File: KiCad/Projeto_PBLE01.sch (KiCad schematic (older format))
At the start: 36 parts

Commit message: correção da avaliação cruzada
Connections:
- net Vcc_5v: no longer Porta_USB1.1 (VBUS)
- no-connect marks 3 -> 4
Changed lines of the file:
@@
 Wire Wire Line
 	1200 6100 1200 5850
-Text GLabel 1800 5250 2    50   Input ~ 0
-Vcc_5v
-Wire Wire Line
-	1800 5250 1500 5250
 Wire Notes Line
 	5950 4850 5950 6500
@@
 Wire Wire Line
 	10050 5950 10300 5950
+NoConn ~ 1500 5250
 $EndSCHEMATC

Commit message: Finalização do esquemático
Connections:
- net Vbus_Externo: now reaches Porta_USB1.1 (VBUS)
- no-connect marks 4 -> 3
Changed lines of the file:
@@
 Text Label 8950 1650 2    50   ~ 0
 USB_R_Led
-$Sheet
-S 9050 850  1250 1000
-U 60BE4F2F
-F0 "Conversor_UART_USB" 50
-F1 "Conversor_UART_USB.sch" 50
-F2 "Rx" I L 9050 1050 50
-F3 "Tx" O L 9050 1150 50
-F4 "RTS" B L 9050 1250 50
-F5 "CTS" B L 9050 1350 50
-F6 "Rx_LED" B L 9050 1650 50
-F7 "Tx_LED" B L 9050 1750 50
-F8 "D-" B R 10300 1150 50
-F9 "D+" B R 10300 1000 50
-$EndSheet
 Wire Wire Line
 	8700 1350 9050 1350
@@
 Wire Wire Line
 	10050 5950 10300 5950
-NoConn ~ 1500 5250
+$Sheet
+S 9050 850  1250 1000
+U 60BE4F2F
+F0 "Conversor_UART_USB" 50
+F1 "Conversor_UART_USB.sch" 50
+F2 "Rx" I L 9050 1050 50
+F3 "Tx" O L 9050 1150 50
+F4 "RTS" B L 9050 1250 50
+F5 "CTS" B L 9050 1350 50
+F6 "Rx_LED" B L 9050 1650 50
+F7 "Tx_LED" B L 9050 1750 50
+F8 "D-" B R 10300 1150 50
+F9 "D+" B R 10300 1000 50
+F10 "Vbus" U R 10300 1650 50
+$EndSheet
+Text Label 10350 1650 0    50   ~ 0
+Vbus_Externo
+Wire Wire Line
+	10300 1650 10350 1650
+Text Label 1700 5250 0    50   ~ 0
+Vbus_Externo
+Wire Wire Line
+	1500 5250 1700 5250
 $EndSCHEMATC

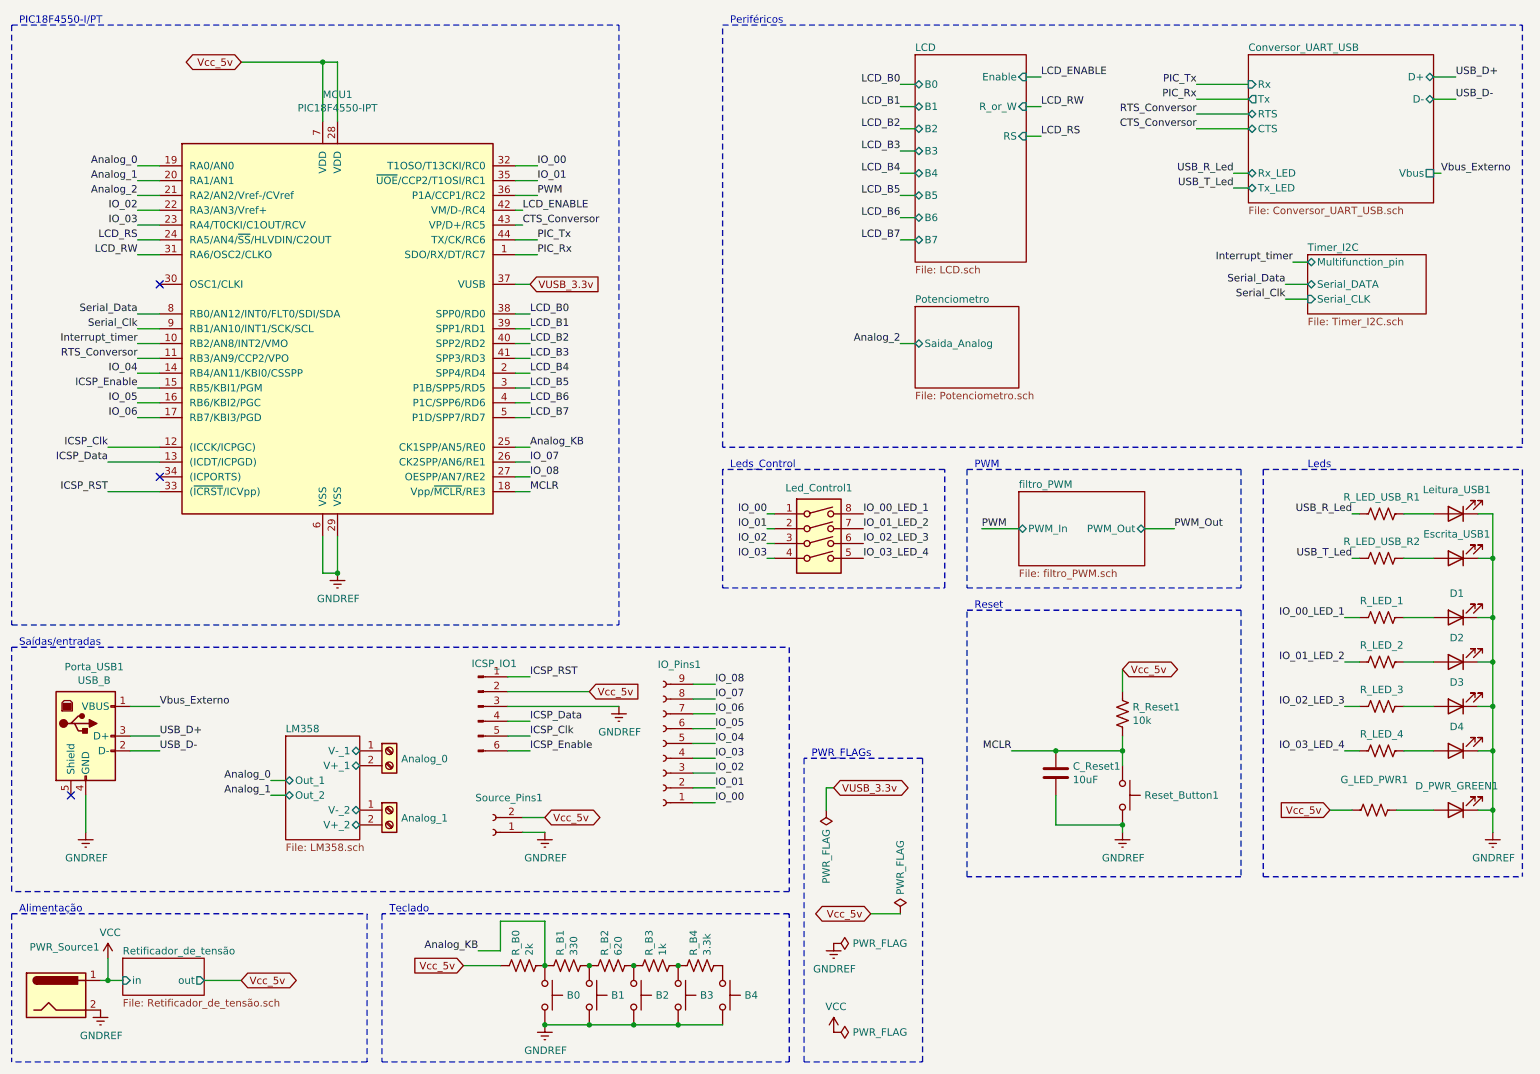
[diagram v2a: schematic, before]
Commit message: adição departe dos footprints
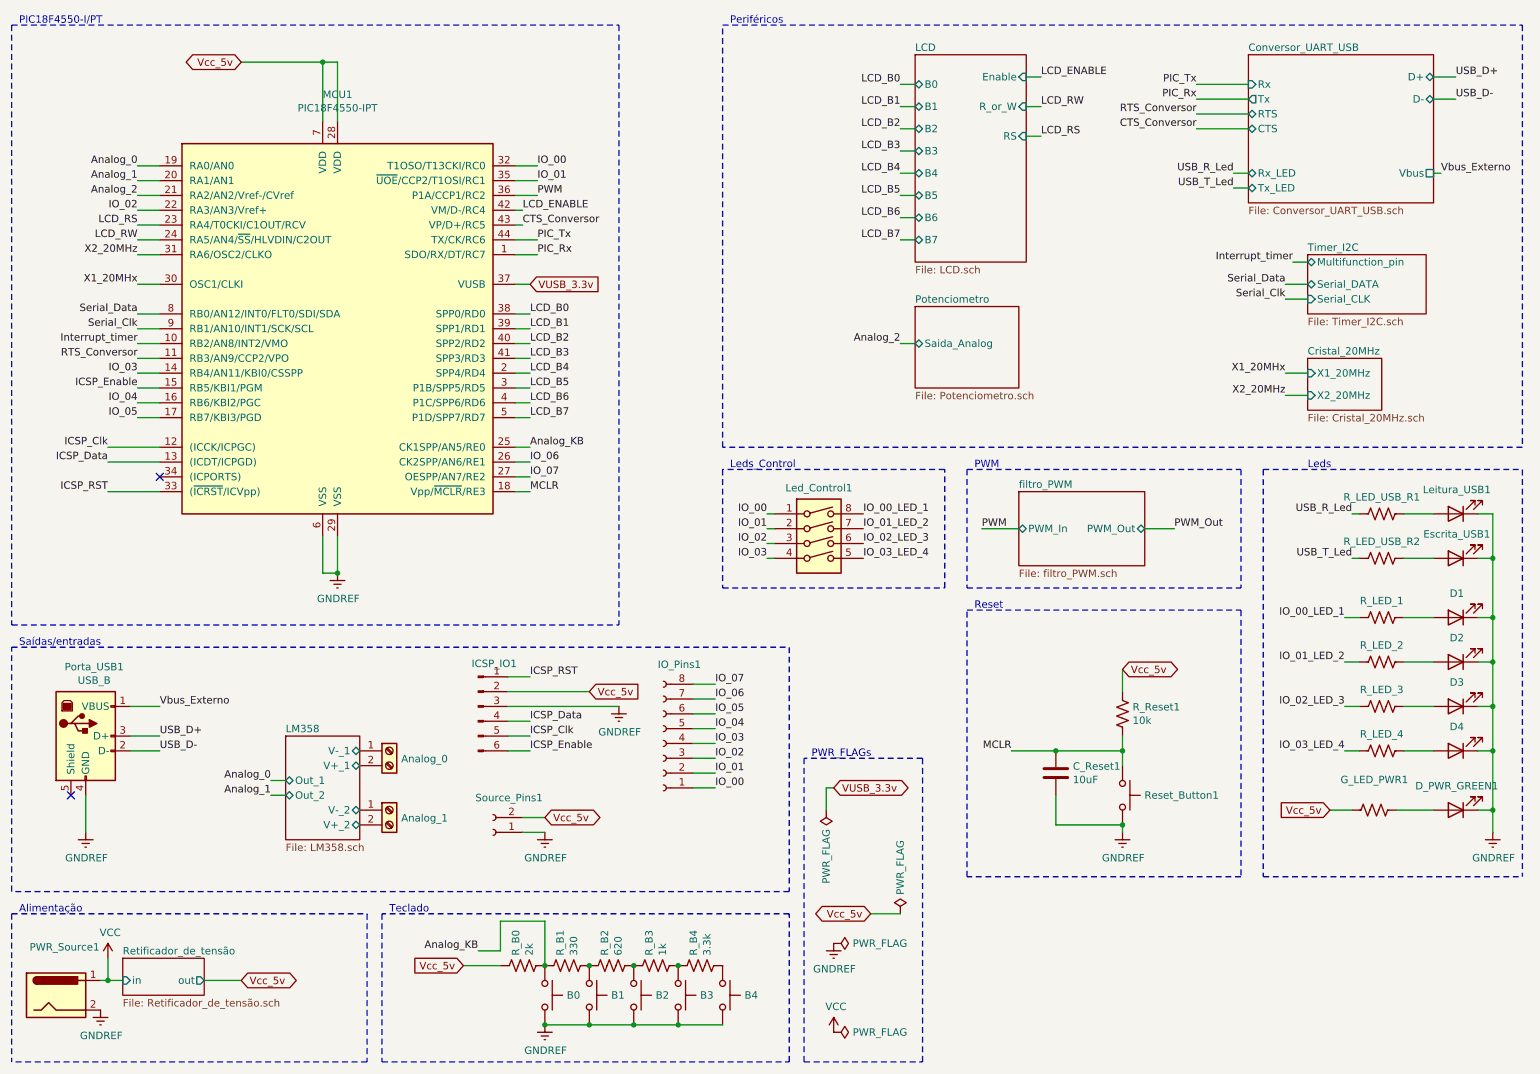
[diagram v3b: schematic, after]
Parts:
- removed IO_Pins1: Conn_01x09_Female, symbol Connector:Conn_01x09_Female
- added IO_Pins1: Conn_01x08_Female, Connector_PinHeader_1.00mm:PinHeader_1x08_P1.00mm_Vertical, symbol Connector:Conn_01x08_Female
- B0, B1, B2, B3, B4: footprint (none) -> Button_Switch_THT:SW_PUSH_6mm
- ICSP_IO1: footprint (none) -> Connector_PinHeader_1.00mm:PinHeader_1x06_P1.00mm_Vertical
- Porta_USB1: footprint (none) -> Connector_USB:USB_B_OST_USB-B1HSxx_Horizontal
- R_B0, R_B1, R_B2, R_B3, R_B4, R_LED_1, R_LED_2, R_LED_3, R_LED_4, R_LED_USB_R1, R_LED_USB_R2, R_Reset1, Reset_Button1: footprint (none) -> Resistor_SMD:R_0805_2012Metric
- Source_Pins1: footprint (none) -> Connector_PinHeader_1.00mm:PinHeader_1x02_P1.00mm_Vertical
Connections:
- net IO_08 is gone; now on net IO_07: MCU1.27 (OESPP/AN7/RE2)
- net IO_00: now also IO_Pins1.1 (Pin_1)
- net IO_01: now also IO_Pins1.2 (Pin_2)
- net IO_02: now also IO_Pins1.3 (Pin_3)
- net IO_03: now also MCU1.14 (RB4/AN11/KBI0/CSSPP), IO_Pins1.4 (Pin_4); no longer MCU1.23 (RA4/T0CKI/C1OUT/RCV)
- net IO_04: now also MCU1.16 (RB6/KBI2/PGC), IO_Pins1.5 (Pin_5); no longer MCU1.14 (RB4/AN11/KBI0/CSSPP)
- net IO_05: now also MCU1.17 (RB7/KBI3/PGD), IO_Pins1.6 (Pin_6); no longer MCU1.16 (RB6/KBI2/PGC)
- net IO_06: now also MCU1.26 (CK2SPP/AN6/RE1), IO_Pins1.7 (Pin_7); no longer MCU1.17 (RB7/KBI3/PGD)
- net IO_07: now also IO_Pins1.8 (Pin_8); no longer MCU1.26 (CK2SPP/AN6/RE1)
- net LCD_RS: now also MCU1.23 (RA4/T0CKI/C1OUT/RCV); no longer MCU1.24 (RA5/AN4/~SS~/HLVDIN/C2OUT)
- net LCD_RW: now also MCU1.24 (RA5/AN4/~SS~/HLVDIN/C2OUT); no longer MCU1.31 (RA6/OSC2/CLKO)
- net X1_20MHx: now reaches MCU1.30 (OSC1/CLKI)
- new net X2_20MHz: MCU1.31 (RA6/OSC2/CLKO)
- no-connect marks 3 -> 2
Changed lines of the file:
@@
 $Descr A4 11693 8268
 encoding utf-8
-Sheet 1 9
+Sheet 1 10
 Title ""
 Date ""
@@
 F 0 "Porta_USB1" H 1257 5917 50  0000 C CNN
 F 1 "USB_B" H 1257 5826 50  0000 C CNN
-F 2 "" H 1350 5400 50  0001 C CNN
+F 2 "Connector_USB:USB_B_OST_USB-B1HSxx_Horizontal" H 1350 5400 50  0001 C CNN
 F 3 " ~" H 1350 5400 50  0001 C CNN
 	1    1200 5450
@@
 F 0 "R_LED_USB_R1" V 9837 3950 50  0000 C CNN
 F 1 "100" V 9837 3950 50  0001 C CNN
-F 2 "" V 9990 3940 50  0001 C CNN
+F 2 "Resistor_SMD:R_0805_2012Metric" V 9990 3940 50  0001 C CNN
 F 3 "~" H 9950 3950 50  0001 C CNN
 	1    9950 3950
@@
 F 0 "R_Reset1" H 8268 5346 50  0000 L CNN
 F 1 "10k" H 8268 5255 50  0000 L CNN
-F 2 "" V 8240 5290 50  0001 C CNN
+F 2 "Resistor_SMD:R_0805_2012Metric" V 8240 5290 50  0001 C CNN
 F 3 "~" H 8200 5300 50  0001 C CNN
 	1    8200 5300
@@
 F 0 "Reset_Button1" V 8200 5998 50  0000 L CNN
 F 1 "SW_Push" V 8245 5998 50  0001 L CNN
-F 2 "" H 8200 6050 50  0001 C CNN
+F 2 "Resistor_SMD:R_0805_2012Metric" H 8200 6050 50  0001 C CNN
 F 3 "~" H 8200 6050 50  0001 C CNN
 	1    8200 5850
@@
 F 0 "R_LED_USB_R2" V 9837 4250 50  0000 C CNN
 F 1 "100" V 9837 4250 50  0001 C CNN
-F 2 "" V 9990 4240 50  0001 C CNN
+F 2 "Resistor_SMD:R_0805_2012Metric" V 9990 4240 50  0001 C CNN
 F 3 "~" H 9950 4250 50  0001 C CNN
 	1    9950 4250
@@
 F 0 "B0" V 4300 7348 50  0000 L CNN
 F 1 "SW_Push" V 4345 7348 50  0001 L CNN
-F 2 "" H 4300 7400 50  0001 C CNN
+F 2 "Button_Switch_THT:SW_PUSH_6mm" H 4300 7400 50  0001 C CNN
 F 3 "~" H 4300 7400 50  0001 C CNN
 	1    4300 7200
@@
 F 0 "B1" V 4600 7348 50  0000 L CNN
 F 1 "SW_Push" V 4645 7348 50  0001 L CNN
-F 2 "" H 4600 7400 50  0001 C CNN
+F 2 "Button_Switch_THT:SW_PUSH_6mm" H 4600 7400 50  0001 C CNN
 F 3 "~" H 4600 7400 50  0001 C CNN
 	1    4600 7200
@@
 F 0 "B2" V 4900 7348 50  0000 L CNN
 F 1 "SW_Push" V 4945 7348 50  0001 L CNN
-F 2 "" H 4900 7400 50  0001 C CNN
+F 2 "Button_Switch_THT:SW_PUSH_6mm" H 4900 7400 50  0001 C CNN
 F 3 "~" H 4900 7400 50  0001 C CNN
 	1    4900 7200
@@
 F 0 "B3" V 5200 7348 50  0000 L CNN
 F 1 "SW_Push" V 5245 7348 50  0001 L CNN
-F 2 "" H 5200 7400 50  0001 C CNN
+F 2 "Button_Switch_THT:SW_PUSH_6mm" H 5200 7400 50  0001 C CNN
 F 3 "~" H 5200 7400 50  0001 C CNN
 	1    5200 7200
@@
 F 0 "B4" V 5500 7348 50  0000 L CNN
 F 1 "SW_Push" V 5545 7348 50  0001 L CNN
-F 2 "" H 5500 7400 50  0001 C CNN
+F 2 "Button_Switch_THT:SW_PUSH_6mm" H 5500 7400 50  0001 C CNN
 F 3 "~" H 5500 7400 50  0001 C CNN
 	1    5500 7200
@@
 F 0 "R_B1" H 4518 7046 50  0000 L CNN
 F 1 "330" H 4518 6955 50  0000 L CNN
-F 2 "" V 4490 6990 50  0001 C CNN
+F 2 "Resistor_SMD:R_0805_2012Metric" V 4490 6990 50  0001 C CNN
 F 3 "~" H 4450 7000 50  0001 C CNN
 	1    4450 7000
@@
 F 0 "R_B2" H 4818 7046 50  0000 L CNN
 F 1 "620" H 4818 6955 50  0000 L CNN
-F 2 "" V 4790 6990 50  0001 C CNN
+F 2 "Resistor_SMD:R_0805_2012Metric" V 4790 6990 50  0001 C CNN
 F 3 "~" H 4750 7000 50  0001 C CNN
 	1    4750 7000
@@
 F 0 "R_B3" H 5118 7046 50  0000 L CNN
 F 1 "1k" H 5118 6955 50  0000 L CNN
-F 2 "" V 5090 6990 50  0001 C CNN
+F 2 "Resistor_SMD:R_0805_2012Metric" V 5090 6990 50  0001 C CNN
 F 3 "~" H 5050 7000 50  0001 C CNN
 	1    5050 7000
@@
 F 0 "R_B4" H 5418 7046 50  0000 L CNN
 F 1 "3.3k" H 5418 6955 50  0000 L CNN
-F 2 "" V 5390 6990 50  0001 C CNN
+F 2 "Resistor_SMD:R_0805_2012Metric" V 5390 6990 50  0001 C CNN
 F 3 "~" H 5350 7000 50  0001 C CNN
 	1    5350 7000
@@
 F 0 "R_B0" H 4218 7046 50  0000 L CNN
 F 1 "2k" H 4218 6955 50  0000 L CNN
-F 2 "" V 4190 6990 50  0001 C CNN
+F 2 "Resistor_SMD:R_0805_2012Metric" V 4190 6990 50  0001 C CNN
 F 3 "~" H 4150 7000 50  0001 C CNN
 	1    4150 7000
@@
 F 0 "R_LED_1" V 9837 4650 50  0000 C CNN
 F 1 "100" V 9837 4650 50  0001 C CNN
-F 2 "" V 9990 4640 50  0001 C CNN
+F 2 "Resistor_SMD:R_0805_2012Metric" V 9990 4640 50  0001 C CNN
 F 3 "~" H 9950 4650 50  0001 C CNN
 	1    9950 4650
@@
 F 0 "R_LED_2" V 9837 4950 50  0000 C CNN
 F 1 "100" V 9837 4950 50  0001 C CNN
-F 2 "" V 9990 4940 50  0001 C CNN
+F 2 "Resistor_SMD:R_0805_2012Metric" V 9990 4940 50  0001 C CNN
 F 3 "~" H 9950 4950 50  0001 C CNN
 	1    9950 4950
@@
 F 0 "R_LED_3" V 9837 5250 50  0000 C CNN
 F 1 "100" V 9837 5250 50  0001 C CNN
-F 2 "" V 9990 5240 50  0001 C CNN
+F 2 "Resistor_SMD:R_0805_2012Metric" V 9990 5240 50  0001 C CNN
 F 3 "~" H 9950 5250 50  0001 C CNN
 	1    9950 5250
@@
 F 0 "R_LED_4" V 9837 5550 50  0000 C CNN
 F 1 "100" V 9837 5550 50  0001 C CNN
-F 2 "" V 9990 5540 50  0001 C CNN
+F 2 "Resistor_SMD:R_0805_2012Metric" V 9990 5540 50  0001 C CNN
 F 3 "~" H 9950 5550 50  0001 C CNN
 	1    9950 5550
@@
 F 0 "Source_Pins1" H 3842 5867 50  0000 C CNN
 F 1 "Conn_01x02_Female" H 3842 5866 50  0001 C CNN
-F 2 "" H 3950 6100 50  0001 C CNN
+F 2 "Connector_PinHeader_1.00mm:PinHeader_1x02_P1.00mm_Vertical" H 3950 6100 50  0001 C CNN
 F 3 "~" H 3950 6100 50  0001 C CNN
 	1    3950 6100
@@
 Wire Wire Line
 	1550 1600 1700 1600
-Text Label 1550 3000 2    50   ~ 0
+Text Label 1550 3200 2    50   ~ 0
 IO_04
-Text Label 1550 3200 2    50   ~ 0
+Text Label 1550 3300 2    50   ~ 0
 IO_05
-Text Label 1550 3300 2    50   ~ 0
+Text Label 4200 3600 0    50   ~ 0
 IO_06
 Wire Wire Line
-	1550 3000 1700 3000
+	1550 3200 1700 3200
+Text Label 1550 2000 2    50   ~ 0
+LCD_RS
 Text Label 1550 2100 2    50   ~ 0
-LCD_RS
-Text Label 1550 2200 2    50   ~ 0
 LCD_RW
 Wire Wire Line
+	1550 2000 1700 2000
+Wire Wire Line
 	1550 2100 1700 2100
-Wire Wire Line
-	1550 2200 1700 2200
 Wire Wire Line
 	4100 1900 4150 1900
@@
 Wire Wire Line
 	1550 3100 1700 3100
-NoConn ~ 1700 2400
 Text Label 4200 3500 0    50   ~ 0
 Analog_KB
@@
 	4100 3500 4200 3500
 Wire Wire Line
-	1550 2000 1700 2000
-Wire Wire Line
-	1550 3200 1700 3200
-Text Label 4200 3600 0    50   ~ 0
-IO_07
-Wire Wire Line
-	4100 3600 4200 3600
+	1550 3000 1700 3000
 Wire Wire Line
 	1550 3300 1700 3300
 Text Label 4200 3700 0    50   ~ 0
-IO_08
+IO_07
+Wire Wire Line
+	4100 3700 4200 3700
 Text Label 4250 1800 0    50   ~ 0
 PWM
@@
 	1    0    0    -1
 $EndComp
+Text Label 5450 5700 0    50   ~ 0
+IO_01
 Text Label 5450 5800 0    50   ~ 0
-IO_01
-Text Label 5450 5900 0    50   ~ 0
 IO_00
-Text Label 5450 5700 0    50   ~ 0
+Text Label 5450 5600 0    50   ~ 0
 IO_02
 Wire Wire Line
-	5450 5900 5300 5900
-Wire Wire Line
 	5450 5800 5300 5800
 Wire Wire Line
 	5450 5700 5300 5700
-Text Label 5450 5600 0    50   ~ 0
+Wire Wire Line
+	5450 5600 5300 5600
+Text Label 5450 5500 0    50   ~ 0
 IO_03
-Text Label 5450 5500 0    50   ~ 0
+Text Label 5450 5400 0    50   ~ 0
 IO_04
-Text Label 5450 5400 0    50   ~ 0
+Text Label 5450 5300 0    50   ~ 0
 IO_05
 Wire Wire Line
-	5300 5600 5450 5600
-Wire Wire Line
 	5300 5500 5450 5500
 Wire Wire Line
 	5300 5400 5450 5400
-Text Label 5450 5300 0    50   ~ 0
-IO_06
 Wire Wire Line
 	5300 5300 5450 5300
 Text Label 5450 5200 0    50   ~ 0
+IO_06
+Wire Wire Line
+	5300 5200 5450 5200
+Text Label 5450 5100 0    50   ~ 0
 IO_07
 Wire Wire Line
-	5300 5200 5450 5200
+	5300 5100 5450 5100
 Text Label 4200 5550 0    50   ~ 0
 ICSP_Enable
@@
 F 0 "ICSP_IO1" H 3958 5539 50  0000 C CNN
 F 1 "Conn_01x06_Male" H 3958 5540 50  0001 C CNN
-F 2 "" H 3850 5250 50  0001 C CNN
+F 2 "Connector_PinHeader_1.00mm:PinHeader_1x06_P1.00mm_Vertical" H 3850 5250 50  0001 C CNN
 F 3 "~" H 3850 5250 50  0001 C CNN
 	1    3850 5250
@@
 Text Label 1550 1900 2    50   ~ 0
 IO_02
-Text Label 1550 2000 2    50   ~ 0
+Text Label 1550 3000 2    50   ~ 0
 IO_03
-$Comp
-L Connector:Conn_01x09_Female IO_Pins1
-U 1 1 610BFF1D
-P 5100 5500
-F 0 "IO_Pins1" H 4992 4967 50  0000 C CNN
-F 1 "Conn_01x09_Female" H 4992 4966 50  0001 C CNN
-F 2 "" H 5100 5500 50  0001 C CNN
-F 3 "~" H 5100 5500 50  0001 C CNN
-	1    5100 5500
-	-1   0    0    1
-$EndComp
-Text Label 5450 5100 0    50   ~ 0
-IO_08
-Wire Wire Line
-	5450 5100 5300 5100
 $Sheet
 S 2550 5450 500  700
@@
 F7 "Out_1" B L 2550 5750 50
 $EndSheet
-Wire Wire Line
-	4100 3700 4200 3700
 Wire Wire Line
 	4100 1800 4250 1800
@@
 Wire Wire Line
 	1500 5250 1700 5250
+$Comp
+L Connector:Conn_01x08_Female IO_Pins1
+U 1 1 60E4B780
+P 5100 5500
+F 0 "IO_Pins1" H 4992 4967 50  0000 C CNN
+F 1 "Conn_01x08_Female" H 4992 4966 50  0001 C CNN
+F 2 "Connector_PinHeader_1.00mm:PinHeader_1x08_P1.00mm_Vertical" H 5100 5500 50  0001 C CNN
+F 3 "~" H 5100 5500 50  0001 C CNN
+	1    5100 5500
+	-1   0    0    1
+$EndComp
+Wire Wire Line
+	4100 3600 4200 3600
+$Sheet
+S 9450 2900 500  350
+U 60ED601E
+F0 "Cristal_20MHz" 50
+F1 "Cristal_20MHz.sch" 50
+F2 "X1_20MHz" I L 9450 3000 50
+F3 "X2_20MHz" I L 9450 3150 50
+$EndSheet
+Text Label 9300 3000 2    50   ~ 0
+X1_20MHx
+Text Label 9300 3150 2    50   ~ 0
+X2_20MHz
+Wire Wire Line
+	9300 3000 9450 3000
+Wire Wire Line
+	9300 3150 9450 3150
+Text Label 1550 2400 2    50   ~ 0
+X1_20MHx
+Text Label 1550 2200 2    50   ~ 0
+X2_20MHz
+Wire Wire Line
+	1550 2400 1700 2400
+Wire Wire Line
+	1550 2200 1700 2200
 $EndSCHEMATC

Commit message: adição de mais footprints
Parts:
- Analog_0, Analog_1: footprint (none) -> TerminalBlock:TerminalBlock_Altech_AK300-2_P5.00mm
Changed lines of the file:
@@
 F 0 "Analog_1" H 3330 5896 50  0000 L CNN
 F 1 "Screw_Terminal_01x02" H 3168 5716 50  0001 C CNN
-F 2 "" H 3250 5950 50  0001 C CNN
+F 2 "TerminalBlock:TerminalBlock_Altech_AK300-2_P5.00mm" H 3250 5950 50  0001 C CNN
 F 3 "~" H 3250 5950 50  0001 C CNN
 	1    3250 5950
@@
 F 0 "Analog_0" H 3330 5496 50  0000 L CNN
 F 1 "Screw_Terminal_01x02" H 3330 5451 50  0001 L CNN
-F 2 "" H 3250 5550 50  0001 C CNN
+F 2 "TerminalBlock:TerminalBlock_Altech_AK300-2_P5.00mm" H 3250 5550 50  0001 C CNN
 F 3 "~" H 3250 5550 50  0001 C CNN
 	1    3250 5550

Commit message: pble_zip
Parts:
- C_Reset1: footprint (none) -> Capacitor_Tantalum_SMD:CP_EIA-3216-18_Kemet-A_Pad1.58x1.35mm_HandSolder
- D1, D3, D4, D_PWR_GREEN1, Escrita_USB1, G_LED_PWR1, Leitura_USB1: footprint (none) -> LED_SMD:LED_1206_3216Metric
- D2: footprint (none) -> LED_SMD:LED_1206_3216Metric_Castellated
- Led_Control1: footprint (none) -> Button_Switch_THT:DIP4PIN
- PWR_Source1: footprint (none) -> Connector_BarrelJack:PJ-002A
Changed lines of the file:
@@
 F 0 "Leitura_USB1" H 10443 3787 50  0000 C CNN
 F 1 "LED" H 10443 3786 50  0001 C CNN
-F 2 "" H 10450 3950 50  0001 C CNN
+F 2 "LED_SMD:LED_1206_3216Metric" H 10450 3950 50  0001 C CNN
 F 3 "~" H 10450 3950 50  0001 C CNN
 	1    10450 3950
@@
 F 0 "Escrita_USB1" H 10443 4087 50  0000 C CNN
 F 1 "LED" H 10443 4086 50  0001 C CNN
-F 2 "" H 10450 4250 50  0001 C CNN
+F 2 "LED_SMD:LED_1206_3216Metric" H 10450 4250 50  0001 C CNN
 F 3 "~" H 10450 4250 50  0001 C CNN
 	1    10450 4250
@@
 F 0 "D3" H 10443 5087 50  0000 C CNN
 F 1 "LED" H 10443 5086 50  0001 C CNN
-F 2 "" H 10450 5250 50  0001 C CNN
+F 2 "LED_SMD:LED_1206_3216Metric" H 10450 5250 50  0001 C CNN
 F 3 "~" H 10450 5250 50  0001 C CNN
 	1    10450 5250
@@
 F 0 "D4" H 10443 5387 50  0000 C CNN
 F 1 "LED" H 10443 5386 50  0001 C CNN
-F 2 "" H 10450 5550 50  0001 C CNN
+F 2 "LED_SMD:LED_1206_3216Metric" H 10450 5550 50  0001 C CNN
 F 3 "~" H 10450 5550 50  0001 C CNN
 	1    10450 5550
@@
 F 0 "D_PWR_GREEN1" H 10443 5787 50  0000 C CNN
 F 1 "G_LED" H 10443 5786 50  0001 C CNN
-F 2 "" H 10450 5950 50  0001 C CNN
+F 2 "LED_SMD:LED_1206_3216Metric" H 10450 5950 50  0001 C CNN
 F 3 "~" H 10450 5950 50  0001 C CNN
 	1    10450 5950
@@
 F 0 "G_LED_PWR1" V 9695 5950 50  0000 C CNN
 F 1 "200" V 9787 5950 50  0001 C CNN
-F 2 "" V 9940 5940 50  0001 C CNN
+F 2 "LED_SMD:LED_1206_3216Metric" V 9940 5940 50  0001 C CNN
 F 3 "~" H 9900 5950 50  0001 C CNN
 	1    9900 5950
@@
 F 0 "PWR_Source1" H 1057 7525 50  0000 C CNN
 F 1 "Jack-DC" H 1057 7434 50  0001 C CNN
-F 2 "" H 1050 7160 50  0001 C CNN
+F 2 "Connector_BarrelJack:PJ-002A" H 1050 7160 50  0001 C CNN
 F 3 "~" H 1050 7160 50  0001 C CNN
 	1    1000 7200
@@
 F 0 "C_Reset1" H 7865 5746 50  0000 L CNN
 F 1 "10uF" H 7865 5655 50  0000 L CNN
-F 2 "" H 7788 5550 50  0001 C CNN
+F 2 "Capacitor_Tantalum_SMD:CP_EIA-3216-18_Kemet-A_Pad1.58x1.35mm_HandSolder" H 7788 5550 50  0001 C CNN
 F 3 "~" H 7750 5700 50  0001 C CNN
 	1    7750 5700
@@
 F 0 "D1" H 10443 4487 50  0000 C CNN
 F 1 "LED" H 10443 4486 50  0001 C CNN
-F 2 "" H 10450 4650 50  0001 C CNN
+F 2 "LED_SMD:LED_1206_3216Metric" H 10450 4650 50  0001 C CNN
 F 3 "~" H 10450 4650 50  0001 C CNN
 	1    10450 4650
@@
 F 0 "D2" H 10443 4787 50  0000 C CNN
 F 1 "LED" H 10443 4786 50  0001 C CNN
-F 2 "" H 10450 4950 50  0001 C CNN
+F 2 "LED_SMD:LED_1206_3216Metric_Castellated" H 10450 4950 50  0001 C CNN
 F 3 "~" H 10450 4950 50  0001 C CNN
 	1    10450 4950
@@
 F 0 "Led_Control1" H 6150 4525 50  0000 C CNN
 F 1 "SW_DIP_x04" H 6150 4526 50  0001 C CNN
-F 2 "" H 6150 4150 50  0001 C CNN
+F 2 "Button_Switch_THT:DIP4PIN" H 6150 4150 50  0001 C CNN
 F 3 "~" H 6150 4150 50  0001 C CNN
 	1    6150 4150
